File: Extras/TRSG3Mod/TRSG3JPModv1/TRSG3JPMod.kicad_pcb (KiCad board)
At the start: 2 copper layers, 17.4 x 30.9 mm, 4 parts, among them J1 CGA, J2 CONN, U1 2332

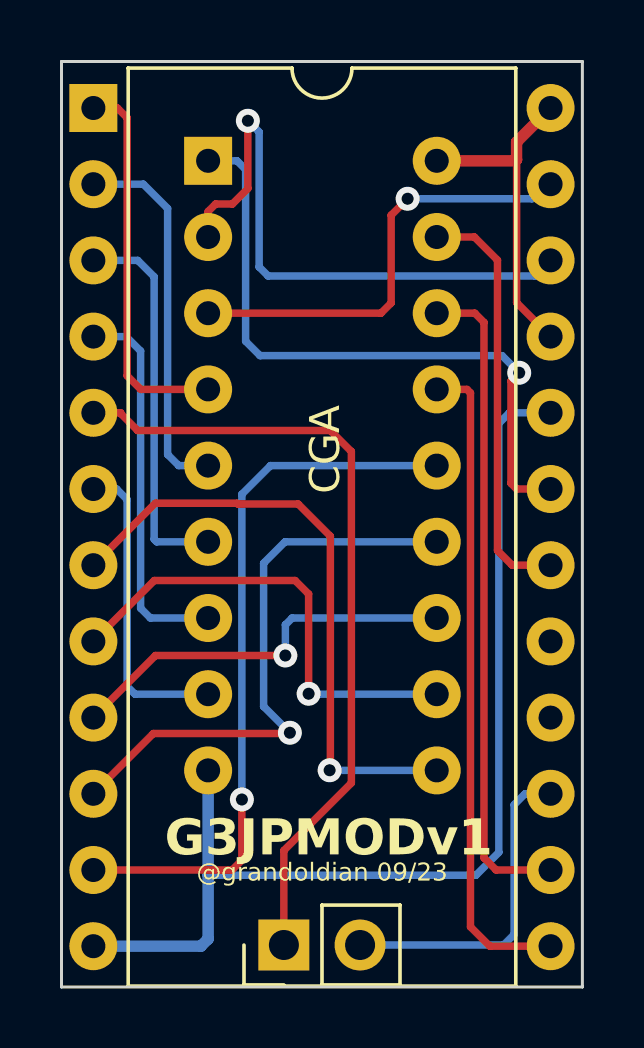
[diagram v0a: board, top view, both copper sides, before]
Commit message: Update TRSG3JPMod and Images
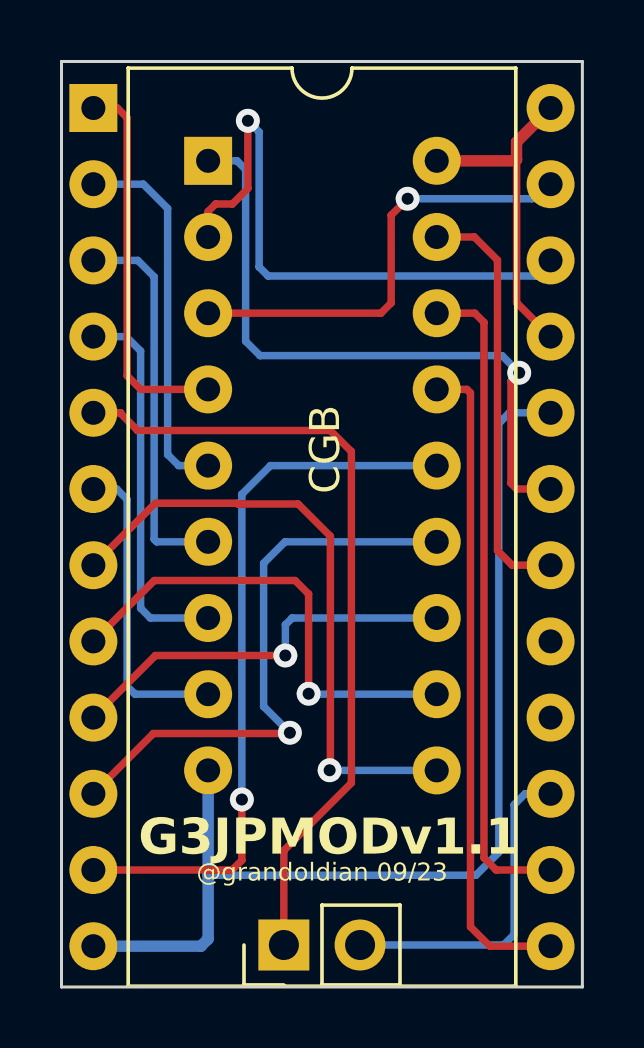
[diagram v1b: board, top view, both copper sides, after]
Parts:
- J1: value CGA -> CGB
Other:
- board text added: "G3JPMODv1.1"
- board text removed: "G3JPMODv1"
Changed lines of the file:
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@@
       (drillshape 0)
       (scaleselection 1)
-      (outputdirectory "TRSG3JPMod_Gerberv1/")
+      (outputdirectory "TRSG3JPMod_Gerberv1.1/")
     )
   )
@@
         (effects (font (size 1 1) (thickness 0.15)))
     )
-    (fp_text value "CGA" (at 3.9 9.62 90) (layer "F.SilkS")
+    (fp_text value "CGB" (at 3.9 9.62 90) (layer "F.SilkS")
         (effects (font (size 1 1) (thickness 0.15)))
     )
@@
     (effects (font (size 0.8 0.8) (thickness 0.1)) (justify left bottom mirror))
   )
-  (gr_text "G3JPMODv1" (at 110.35 81.75) (layer "F.SilkS")
+  (gr_text "G3JPMODv1.1" (at 109.475 81.725) (layer "F.SilkS")
     (effects (font (size 1.2 1.2) (thickness 0.2) bold) (justify left bottom))
   )
